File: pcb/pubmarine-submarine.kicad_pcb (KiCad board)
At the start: 2 copper layers, 100 x 80 mm, 97 parts, among them J1 Screw_Terminal_01x02, J10 Conn_01x02, J11 Conn_01x02, J12 Screw_Terminal_01x02, J13 Conn_01x03, J14 Conn_01x04, J15 Servo1, J16 Servo2, J17 Servo3, J18 Servo4, J19 Conn_01x02, J2 Conn_01x02, J20 Conn_01x02, J21 Conn_01x02, J22 Conn_01x02, J23 Conn_01x02, J24 Conn_01x02, J25 Conn_01x20, J26 Conn_01x20, J27 Conn_01x03, J3 Conn_01x02, J4 Conn_01x02, J5 Conn_01x02, J6 Screw_Terminal_01x02, J7 Screw_Terminal_01x02, J8 Conn_01x02, J9 Conn_01x02, Q1 AO3400A, Q2 AO3400A, Q3 AO3400A, Q4 AO3400A, Q5 AO3400A, Q6 AO3400A, Q7 AO3400A, Q8 AO3400A, U1 Pico, U2 SN74LV1T34DBV, U3 A4950E, U4 A4950E, U5 A4950E, U6 A4950E, U7 MPU-6050

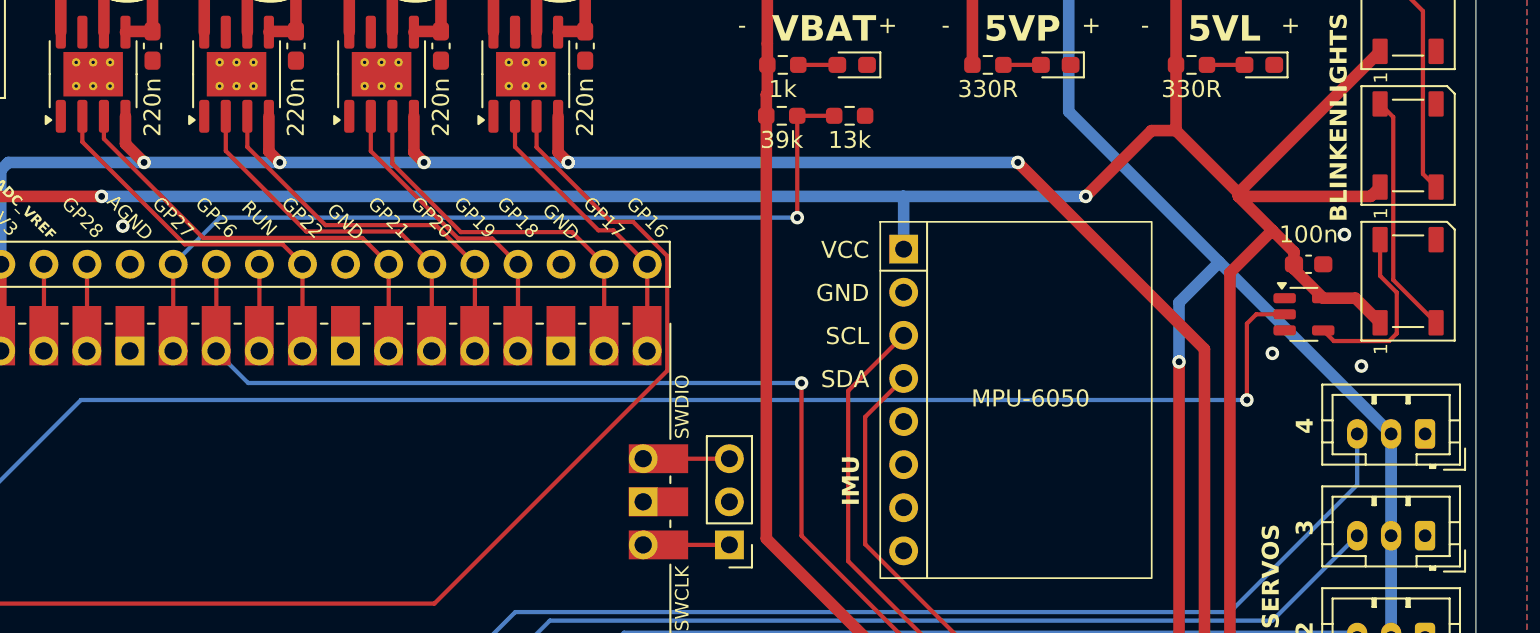
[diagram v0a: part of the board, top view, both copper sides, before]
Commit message: pcb: fix clearances
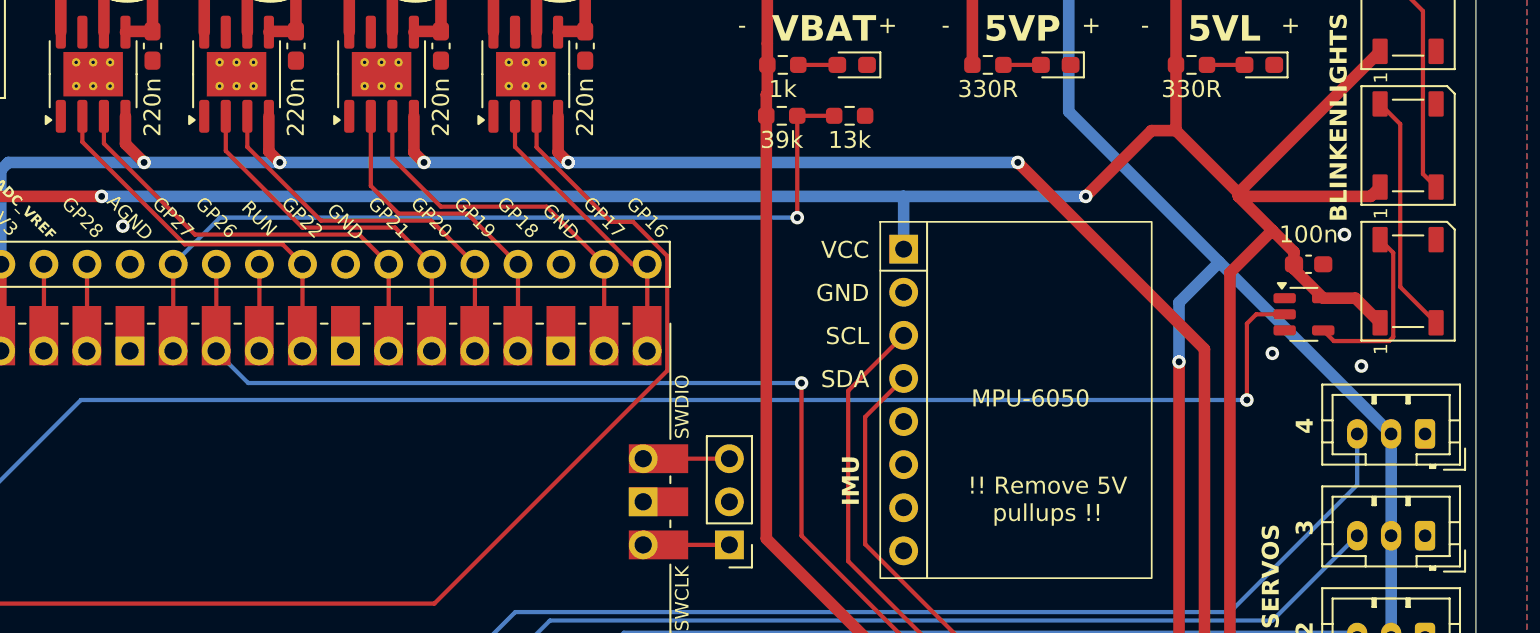
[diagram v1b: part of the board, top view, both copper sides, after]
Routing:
- net IN_Z2: track 18.6 -> 19.8 mm
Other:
- board text added: "!! Remove 5V pullups !!"
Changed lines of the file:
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@@
+		)
+	)
+	(gr_text "!! Remove 5V \npullups !!"
+		(at 124.75 84.25 0)
+		(layer "F.SilkS")
+		(effects
+			(font
+				(size 1 1)
+				(thickness 0.15)
+			)
+			(justify bottom)
 		)
 	)
@@
 	)
 	(segment
-		(start 74.977849 67.448)
-		(end 84.368 67.448)
-		(width 0.25)
-		(layer "F.Cu")
-		(net 14)
-	)
-	(segment
-		(start 69.135 61.605151)
-		(end 74.977849 67.448)
+		(start 74.5 67.25)
+		(end 69.135 61.885)
 		(width 0.25)
 		(layer "F.Cu")
@@
 	)
 	(segment
-		(start 69.135 60.28)
-		(end 69.135 61.605151)
+		(start 85.92 69)
+		(end 84.17 67.25)
 		(width 0.25)
 		(layer "F.Cu")
@@
 	)
 	(segment
-		(start 84.368 67.448)
-		(end 85.92 69)
+		(start 69.135 61.885)
+		(end 69.135 60.28)
+		(width 0.25)
+		(layer "F.Cu")
+		(net 14)
+	)
+	(segment
+		(start 84.17 67.25)
+		(end 74.5 67.25)
 		(width 0.25)
 		(layer "F.Cu")
@@
 	)
 	(segment
-		(start 88.694 66.694)
-		(end 82.194 66.694)
+		(start 81.928 66.428)
+		(end 88.428 66.428)
 		(width 0.25)
 		(layer "F.Cu")
@@
 	)
 	(segment
-		(start 91 69)
-		(end 88.694 66.694)
+		(start 88.428 66.428)
+		(end 91 69)
 		(width 0.25)
 		(layer "F.Cu")
@@
 	)
 	(segment
-		(start 82.194 66.694)
-		(end 77.5875 62.0875)
+		(start 77.5875 62.0875)
+		(end 81.928 66.428)
 		(width 0.25)
 		(layer "F.Cu")
 		(net 15)
+	)
+	(segment
+		(start 86.299 66.839)
+		(end 88.46 69)
+		(width 0.25)
+		(layer "F.Cu")
+		(net 16)
 	)
 	(segment
@@
 	)
 	(segment
-		(start 88.46 69)
-		(end 86.531 67.071)
-		(width 0.25)
-		(layer "F.Cu")
-		(net 16)
-	)
-	(segment
-		(start 86.531 67.071)
-		(end 81.071 67.071)
+		(start 76.3175 62.3175)
+		(end 80.839 66.839)
 		(width 0.25)
 		(layer "F.Cu")
@@
 	)
 	(segment
-		(start 81.071 67.071)
-		(end 76.3175 62.3175)
+		(start 80.839 66.839)
+		(end 86.299 66.839)
 		(width 0.25)
 		(layer "F.Cu")
 		(net 16)
-	)
-	(segment
-		(start 86.135 63.06727)
-		(end 90.174151 67.106421)
-		(width 0.25)
-		(layer "F.Cu")
-		(net 17)
-	)
-	(segment
-		(start 90.174151 67.106421)
-		(end 96.726421 67.106421)
-		(width 0.25)
-		(layer "F.Cu")
-		(net 17)
 	)
 	(segment
@@
 	)
 	(segment
+		(start 86.135 62.75)
+		(end 88.991 65.606)
+		(width 0.25)
+		(layer "F.Cu")
+		(net 17)
+	)
+	(segment
 		(start 98.62 69)
 		(end 98.62 74.1)
@@
 	)
 	(segment
-		(start 96.726421 67.106421)
+		(start 86.135 60.28)
+		(end 86.135 62.75)
+		(width 0.25)
+		(layer "F.Cu")
+		(net 17)
+	)
+	(segment
+		(start 88.991 65.606)
+		(end 95.226 65.606)
+		(width 0.25)
+		(layer "F.Cu")
+		(net 17)
+	)
+	(segment
+		(start 95.226 65.606)
 		(end 98.62 69)
-		(width 0.25)
-		(layer "F.Cu")
-		(net 17)
-	)
-	(segment
-		(start 86.135 60.28)
-		(end 86.135 63.06727)
 		(width 0.25)
 		(layer "F.Cu")
@@
 	)
 	(segment
-		(start 90.016579 67.483421)
-		(end 92.023421 67.483421)
+		(start 84.865 60.28)
+		(end 84.865 64.382)
 		(width 0.25)
 		(layer "F.Cu")
@@
 	)
 	(segment
-		(start 92.023421 67.483421)
+		(start 90.557 66.017)
 		(end 93.54 69)
 		(width 0.25)
@@
 	)
 	(segment
-		(start 84.865 60.28)
-		(end 84.865 62.331842)
+		(start 84.865 64.382)
+		(end 86.5 66.017)
 		(width 0.25)
 		(layer "F.Cu")
@@
 	)
 	(segment
-		(start 84.865 62.331842)
-		(end 90.016579 67.483421)
+		(start 86.5 66.017)
+		(end 90.557 66.017)
 		(width 0.25)
 		(layer "F.Cu")
@@
 	)
 	(segment
+		(start 100.281701 69)
+		(end 101.16 69)
+		(width 0.25)
+		(layer "F.Cu")
+		(net 20)
+	)
+	(segment
 		(start 93.365 62.083299)
-		(end 98.281701 67)
+		(end 100.281701 69)
 		(width 0.25)
 		(layer "F.Cu")
@@
 	)
 	(segment
-		(start 99.16 67)
-		(end 101.16 69)
-		(width 0.25)
-		(layer "F.Cu")
-		(net 20)
-	)
-	(segment
 		(start 93.365 60.28)
 		(end 93.365 62.083299)
@@
 	)
 	(segment
-		(start 98.281701 67)
-		(end 99.16 67)
-		(width 0.25)
-		(layer "F.Cu")
-		(net 20)
-	)
-	(segment
-		(start 145.125 60.325)
+		(start 147.65 72.45)
+		(end 145.537 70.337)
+		(width 0.25)
+		(layer "F.Cu")
+		(net 21)
+	)
+	(segment
+		(start 145.537 70.337)
+		(end 145.537 60.737)
+		(width 0.25)
+		(layer "F.Cu")
+		(net 21)
+	)
+	(segment
+		(start 145.537 60.737)
 		(end 144.35 59.55)
 		(width 0.25)
@@
 	)
 	(segment
-		(start 145.125 69.925)
-		(end 145.125 60.325)
-		(width 0.25)
-		(layer "F.Cu")
-		(net 21)
-	)
-	(segment
-		(start 147.65 72.45)
-		(end 145.125 69.925)
-		(width 0.25)
-		(layer "F.Cu")
-		(net 21)
+		(start 145.126 73.284806)
+		(end 145.126 68.326)
+		(width 0.25)
+		(layer "F.Cu")
+		(net 22)
+	)
+	(segment
+		(start 141.626 73.526)
+		(end 144.884806 73.526)
+		(width 0.25)
+		(layer "F.Cu")
+		(net 22)
+	)
+	(segment
+		(start 144.884806 73.526)
+		(end 145.126 73.284806)
+		(width 0.25)
+		(layer "F.Cu")
+		(net 22)
+	)
+	(segment
+		(start 145.126 68.326)
+		(end 144.35 67.55)
+		(width 0.25)
+		(layer "F.Cu")
+		(net 22)
 	)
 	(segment
 		(start 141 72.9)
-		(end 141.625 73.525)
-		(width 0.25)
-		(layer "F.Cu")
-		(net 22)
-	)
-	(segment
-		(start 144.884392 73.525)
-		(end 145.333421 73.075971)
-		(width 0.25)
-		(layer "F.Cu")
-		(net 22)
-	)
-	(segment
-		(start 145.333421 70.666579)
-		(end 144.35 69.683158)
-		(width 0.25)
-		(layer "F.Cu")
-		(net 22)
-	)
-	(segment
-		(start 141.625 73.525)
-		(end 144.884392 73.525)
-		(width 0.25)
-		(layer "F.Cu")
-		(net 22)
-	)
-	(segment
-		(start 145.333421 73.075971)
-		(end 145.333421 70.666579)
-		(width 0.25)
-		(layer "F.Cu")
-		(net 22)
-	)
-	(segment
-		(start 144.35 69.683158)
-		(end 144.35 67.55)
-		(width 0.25)
-		(layer "F.Cu")
+		(end 141.626 73.526)
+		(width 0.25)
+		(layer "F.Cu")

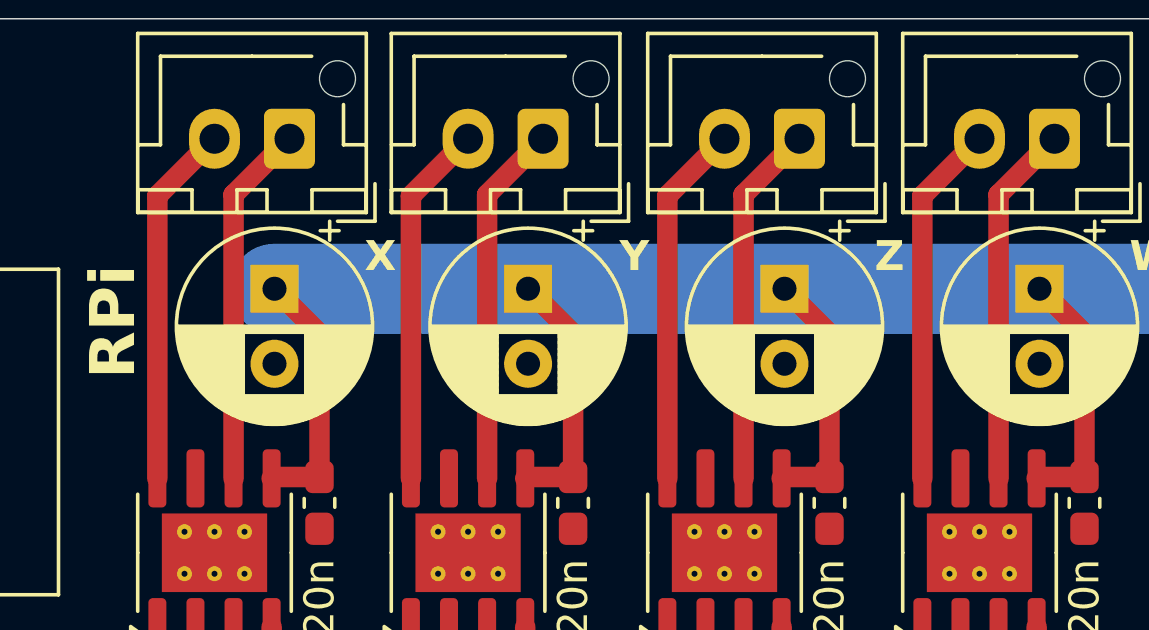
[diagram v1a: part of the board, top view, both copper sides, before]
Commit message: pcb: fix LSS pins, notes for other rev2 changes
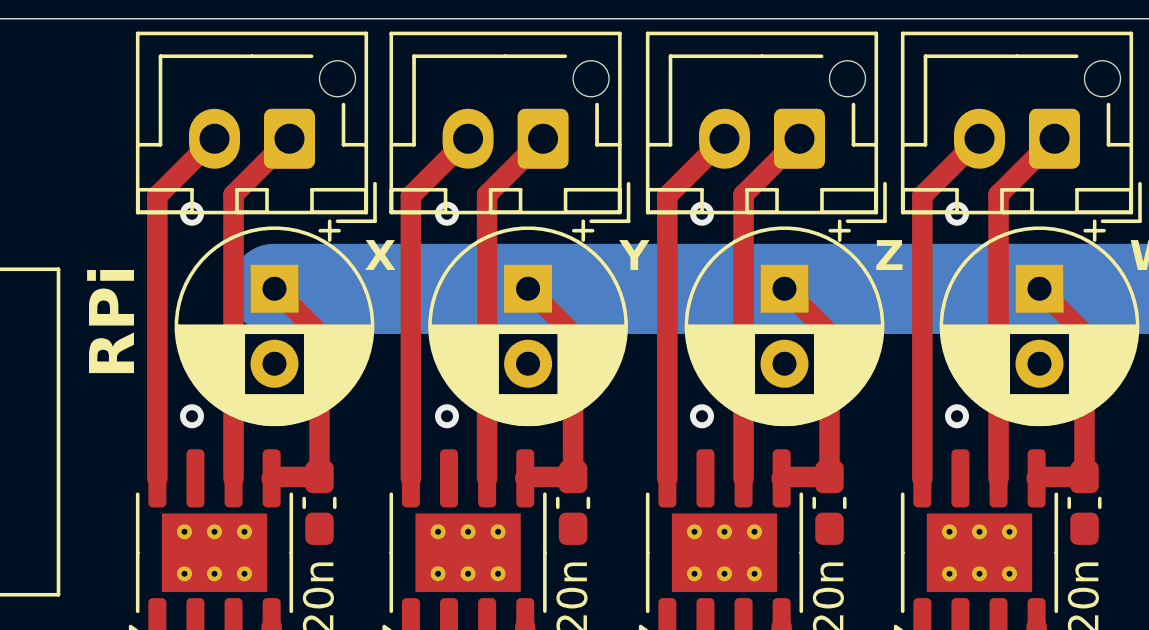
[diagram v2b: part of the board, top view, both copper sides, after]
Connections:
- U3 pad 7: unconnected-(U3-LSS-Pad7) -> GND
- U4 pad 7: unconnected-(U4-LSS-Pad7) -> GND
- U5 pad 7: unconnected-(U5-LSS-Pad7) -> GND
- U6 pad 7: unconnected-(U6-LSS-Pad7) -> GND
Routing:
- net GND: vias 9 -> 17

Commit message: wip: PCB rev2, motors mostly done?
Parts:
- removed C10, C6, C8: 220n, Capacitor_SMD:C_0603_1608Metric_Pad1.08x0.95mm_HandSolder
- removed C11, C5, C7, C9: 100u, Capacitor_THT:CP_Radial_D6.3mm_P2.50mm
- removed J21: Conn_01x02, Connector_JST:JST_XH_B2B-XH-AM_1x02_P2.50mm_Vertical
- removed J27: Conn_01x03, Connector_PinHeader_2.54mm:PinHeader_1x03_P2.54mm_Vertical
- removed U3, U4, U6: A4950E, Package_SO:SOIC-8-1EP_3.9x4.9mm_P1.27mm_EP2.62x3.51mm_ThermalVias
- added C12: 1U, Capacitor_SMD:C_0603_1608Metric_Pad1.08x0.95mm_HandSolder, F.Cu at (71.5, 60.0)
- added C13: 100N, Capacitor_SMD:C_0603_1608Metric_Pad1.08x0.95mm_HandSolder, F.Cu at (81.5, 55.8)
- added C14: 1U, Capacitor_SMD:C_0603_1608Metric_Pad1.08x0.95mm_HandSolder, F.Cu at (73.8, 51.5)
- added C15: 100N, Capacitor_SMD:C_0603_1608Metric_Pad1.08x0.95mm_HandSolder, F.Cu at (75.2, 51.0)
- added C16: 47N, Capacitor_SMD:C_0603_1608Metric_Pad1.08x0.95mm_HandSolder, F.Cu at (71.1, 53.0)
- added C17: 220U, Capacitor_THT:CP_Radial_D6.3mm_P2.50mm, F.Cu at (67.5, 55.5)
- added C18: C, Capacitor_SMD:C_0603_1608Metric_Pad1.08x0.95mm_HandSolder, F.Cu at (76.8, 47.8)
- added C19: C, Capacitor_SMD:C_0603_1608Metric_Pad1.08x0.95mm_HandSolder, F.Cu at (94.5, 47.8)
- added C20: 100N, Capacitor_SMD:C_0603_1608Metric_Pad1.08x0.95mm_HandSolder, F.Cu at (67.5, 52.0)
- added C21: 1U, Capacitor_SMD:C_0603_1608Metric_Pad1.08x0.95mm_HandSolder, F.Cu at (87.2, 60.1)
- added C22: 100N, Capacitor_SMD:C_0603_1608Metric_Pad1.08x0.95mm_HandSolder, F.Cu at (97.2, 55.8)
- added C23: 1U, Capacitor_SMD:C_0603_1608Metric_Pad1.08x0.95mm_HandSolder, F.Cu at (89.4, 51.6)
- added C24: 100N, Capacitor_SMD:C_0603_1608Metric_Pad1.08x0.95mm_HandSolder, F.Cu at (90.9, 51.1)
- added C25: 47N, Capacitor_SMD:C_0603_1608Metric_Pad1.08x0.95mm_HandSolder, F.Cu at (86.8, 53.1)
- added C26: 220U, Capacitor_THT:CP_Radial_D6.3mm_P2.50mm, F.Cu at (102.2, 54.9)
- added JP2: SolderJumper_3_Bridged12, Jumper:SolderJumper-3_P1.3mm_Bridged12_RoundedPad1.0x1.5mm, B.Cu at (74.0, 62.8)
- added JP3: SolderJumper_3_Bridged12, Jumper:SolderJumper-3_P1.3mm_Bridged12_RoundedPad1.0x1.5mm, B.Cu at (77.8, 62.8)
- added JP4: SolderJumper_3_Bridged12, Jumper:SolderJumper-3_P1.3mm_Bridged12_RoundedPad1.0x1.5mm, B.Cu at (89.7, 62.8)
- added JP5: SolderJumper_3_Bridged12, Jumper:SolderJumper-3_P1.3mm_Bridged12_RoundedPad1.0x1.5mm, B.Cu at (93.4, 62.8)
- added Q9: AO3400A, Package_TO_SOT_SMD:SOT-23_Handsoldering, F.Cu at (132.0, 110.5)
- added R26: 470R, Resistor_SMD:R_0603_1608Metric_Pad0.98x0.95mm_HandSolder, F.Cu at (128.5, 104.5)
- added R27: 10k, Resistor_SMD:R_0603_1608Metric_Pad0.98x0.95mm_HandSolder, F.Cu at (125.0, 112.0)
- added R28: 10K, Resistor_SMD:R_0603_1608Metric_Pad0.98x0.95mm_HandSolder, F.Cu at (56.5, 63.0)
- added R29: 330R, Resistor_SMD:R_0603_1608Metric_Pad0.98x0.95mm_HandSolder, F.Cu at (81.5, 60.1)
- added R30: 10K, Resistor_SMD:R_0603_1608Metric_Pad0.98x0.95mm_HandSolder, F.Cu at (69.5, 63.5)
- added R31: 10k, Resistor_SMD:R_0603_1608Metric_Pad0.98x0.95mm_HandSolder, F.Cu at (34.2, 60.8)
- added R32: 330R, Resistor_SMD:R_0603_1608Metric_Pad0.98x0.95mm_HandSolder, F.Cu at (97.2, 60.1)
- added R33: 10K, Resistor_SMD:R_0603_1608Metric_Pad0.98x0.95mm_HandSolder, F.Cu at (85.5, 63.0)
- added SW1: SW_Push, Button_Switch_THT:SW_PUSH_6mm, F.Cu at (65.0, 49.0)
- added U10: DRV8873H, Package_SO:HTSSOP-24-1EP_4.4x7.8mm_P0.65mm_EP3.4x7.8mm_Mask2.44x3.42mm_ThermalVias, F.Cu at (76.5, 57.8)
- added U11: DRV8873H, Package_SO:HTSSOP-24-1EP_4.4x7.8mm_P0.65mm_EP3.4x7.8mm_Mask2.44x3.42mm_ThermalVias, F.Cu at (92.2, 57.8)
- added U9: ADS1015IDGS, Package_SO:TSSOP-10_3x3mm_P0.5mm, F.Cu at (31.5, 61.1)
- C1, C2: value 100u -> 220U
- C3: value 100n -> 100N
- C4: value 220n -> 100N
- J22: value Conn_01x02 -> Conn_01x04; footprint Connector_JST:JST_XH_B2B-XH-AM_1x02_P2.50mm_Vertical -> Connector_PinHeader_2.54mm:PinHeader_1x04_P2.54mm_Vertical
- JP1: value Jumper_2_Bridged -> Jumper_2_Open; footprint Jumper:SolderJumper-2_P1.3mm_Bridged_RoundedPad1.0x1.5mm -> Jumper:SolderJumper-2_P1.3mm_Open_RoundedPad1.0x1.5mm; moved to B.Cu
- U1: footprint MCU_RaspberryPi_and_Boards:RPi_Pico_SMD_TH -> pubmarine-submarine:RPi_Pico_SMD_TH
- U5: value A4950E -> ER_OLEDM0.91_1x-I2C; footprint Package_SO:SOIC-8-1EP_3.9x4.9mm_P1.27mm_EP2.62x3.51mm_ThermalVias -> Display:ER_OLEDM0.91_1x-I2C
- moved R5 106.9 mm to (15.2, 15.5), turned to 0 degrees
- moved J22 55.7 mm to (124.0, 92.5), turned to 90 degrees
- moved C4 43.5 mm to (28.8, 61.0), turned to 90 degrees
- moved U5 22.8 mm to (107.0, 65.5), turned to 0 degrees
- moved J29 16.2 mm to (95.7, 44.0)
- moved J28 7.00 mm to (78.0, 44.0)
- moved U7 5.15 mm to (120.8, 65.6)
- moved JP1 2.75 mm to (55.5, 63.0), turned to 90 degrees
- renumbered J19 to J28, J20 to J29
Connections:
- net /GPIO28_ADC2 renamed ~{FAULT_A}
- net /RUN renamed RUN
- net IN_W1 renamed Net-(J25-Pin_2)
- net IN_W2 renamed IN_B2
- net IN_X1 renamed Net-(J26-Pin_14)
- net IN_X2 renamed ~{SLEEP_B}
- net IN_Y1 renamed IN_A1
- net IN_Y2 renamed Net-(J26-Pin_15)
- net Net-(J26-Pin_2) renamed VSYS
- C4 pad 1: +12V -> +3.3V
- J22 pad 1: /WA -> +3.3V
- J22 pad 2: /WB -> SDA
- J23 pad 2: GND -> Net-(J23-Pin_2)
- J24 pad 2: GND -> Net-(J23-Pin_2)
- J26 pad 10: SENS1 -> ~{FAULT_B}
- J26 pad 17: IN_Z2 -> IN_A2
- J26 pad 19: IN_Z1 -> IN_B1
- J26 pad 9: BAT_SENS -> ~{SLEEP_A}
- J28 pad 1: /XA -> /A2
- J28 pad 2: /XB -> /A1
- J29 pad 1: /YA -> /B2
- J29 pad 2: /YB -> /B1
- U1 pad 22: IN_Z1 -> IN_B1
- U1 pad 24: IN_Z2 -> IN_A2
- U1 pad 31: SENS1 -> ~{FAULT_B}
- U1 pad 32: BAT_SENS -> ~{SLEEP_A}
- U5 pad 2: IN_Z2 -> +3.3V
- U5 pad 3: IN_Z1 -> SCL
- U5 pad 4: +3.3V -> SDA
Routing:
- net +5VP: track 293.8 -> 0.00 mm, vias 9 -> 0
- net +5VL: track 193.9 -> 13.6 mm, vias 2 -> 0
- net +12V: track 172.1 -> 22.0 mm, vias 1 -> 8
- net SDA: track 129.2 -> 5.11 mm, vias 2 -> 0
- net SCL: track 127.0 -> 5.11 mm, vias 2 -> 0
- net +3.3V: track 127.4 -> 19.8 mm, vias 5 -> 0
- net LED_DATA: track 101.8 -> 5.11 mm, vias 1 -> 0
- net GND: track 0.00 -> 94.2 mm, vias 17 -> 2
- net SENS1: track 86.7 -> 0.00 mm, vias 3 -> 0
- net Net-(J25-Pin_2): track 78.6 -> 5.11 mm
- net SV4: track 64.2 -> 5.11 mm
- net SV3: track 57.4 -> 5.11 mm
- net BAT_SENS: track 51.2 -> 0.00 mm, vias 1 -> 0
- net RUN: track 5.11 -> 51.4 mm
- net SV2: track 50.1 -> 5.11 mm
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- added copper zone on In2.Cu, net +12V
- added copper zone on In1.Cu, net GND
- added copper zone on In2.Cu, net GND
- removed copper zone on B.Cu, net GND
- removed copper zone on F.Cu, net GND
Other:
- copper layers 2 -> 4
- board text added: "A"
- board text added: "B"
- board text added: "The PubSubHub revision 2.0 by @DeltaWhy https://github.com/PubmarineSubmarine JLCJLCJLCJLC"
- board text removed: "The PubSubHub revision 1.0 by @DeltaWhy https://github.com/PubmarineSubmarine JLCJLCJLCJLC"
- board text removed: "W"
- board text removed: "X"
- board text removed: "Y"
- board text removed: "Z"
